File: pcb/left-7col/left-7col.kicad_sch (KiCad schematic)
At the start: 54 parts, among them SW1 SW_SPDT_312, SW2 SW_SPST, U1 SuperMini

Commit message: Change horizontal spacing and add nice!view to left half
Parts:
- added U2: nice!view, strizh_lib:nice_view, symbol strizh_lib:nice_view
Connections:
- net -BATT: now also U2.4 (GND)
- net COL1: now also U1.8 (CS/D5/024); no longer U1.5 (SCK/D2/017)
- net COL2: now also U1.9 (SDA/D6/100); no longer U1.6 (MISO/D3/020)
- net COL3: now also U1.10 (SCL/D7/011); no longer U1.7 (MOSI/D4/022)
- net COL4: now also U1.11 (D8/104); no longer U1.8 (CS/D5/024)
- net COL5: now also U1.12 (D9/106); no longer U1.9 (SDA/D6/100)
- net COL6: now also U1.17 (SCL1/D14/115); no longer U1.10 (SCL/D7/011)
- net COL7: now also U1.18 (A0/D15/002); no longer U1.11 (D8/104)
- net ROW1: now also U1.16 (SDA1/D13/113); no longer U1.15 (D12/111)
- net ROW2: now also U1.15 (D12/111); no longer U1.14 (NFC2/D11/010)
- net ROW3: now also U1.14 (NFC2/D11/010); no longer U1.13 (NFC1/D10/009)
- net ROW4: now also U1.13 (NFC1/D10/009); no longer U1.12 (D9/106)
- net cs: now reaches U1.1 (TX/D1/006)
- net cs: now also U2.5 (CS)
- net +3.3V: now reaches U1.21 (EXT_VCC/013)
- net +3.3V: now also U2.3 (VCC)
- new net mosi: U1.7 (MOSI/D4/022), U2.1 (MOSI)
- new net sck: U1.5 (SCK/D2/017), U2.2 (SCK)
- no-connect marks 36 -> 32

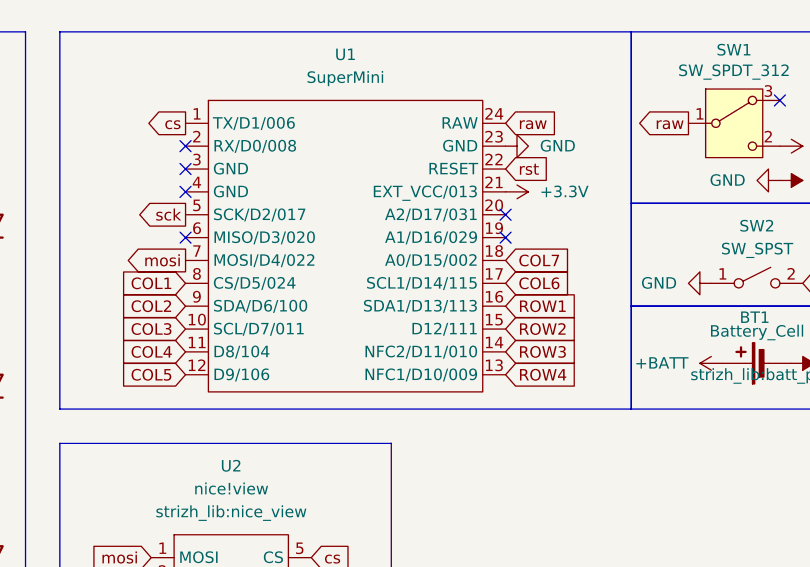
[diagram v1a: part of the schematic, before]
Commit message: Fix pin naming of supermini
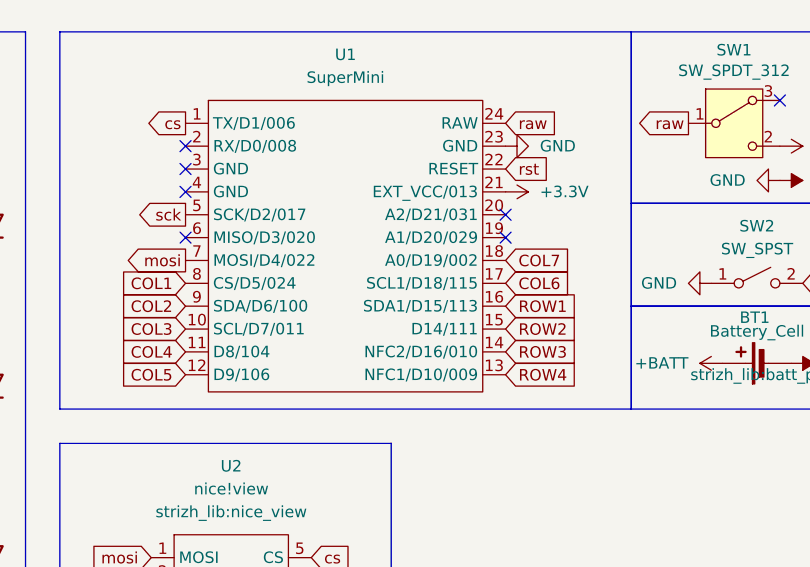
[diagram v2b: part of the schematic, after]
